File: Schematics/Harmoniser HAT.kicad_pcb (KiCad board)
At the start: 2 copper layers, 150 x 75 mm, 34 parts, among them J1 RPi GPIO, J10 Line In, J11 BOB21250-LEFT, J12 BOB21250-RIGHT, J6 I2C Header, J7 PWR, J8 I2S Header, J9 Line In, SW1 RotaryEncoder_Switch, SW2 RotaryEncoder_Switch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

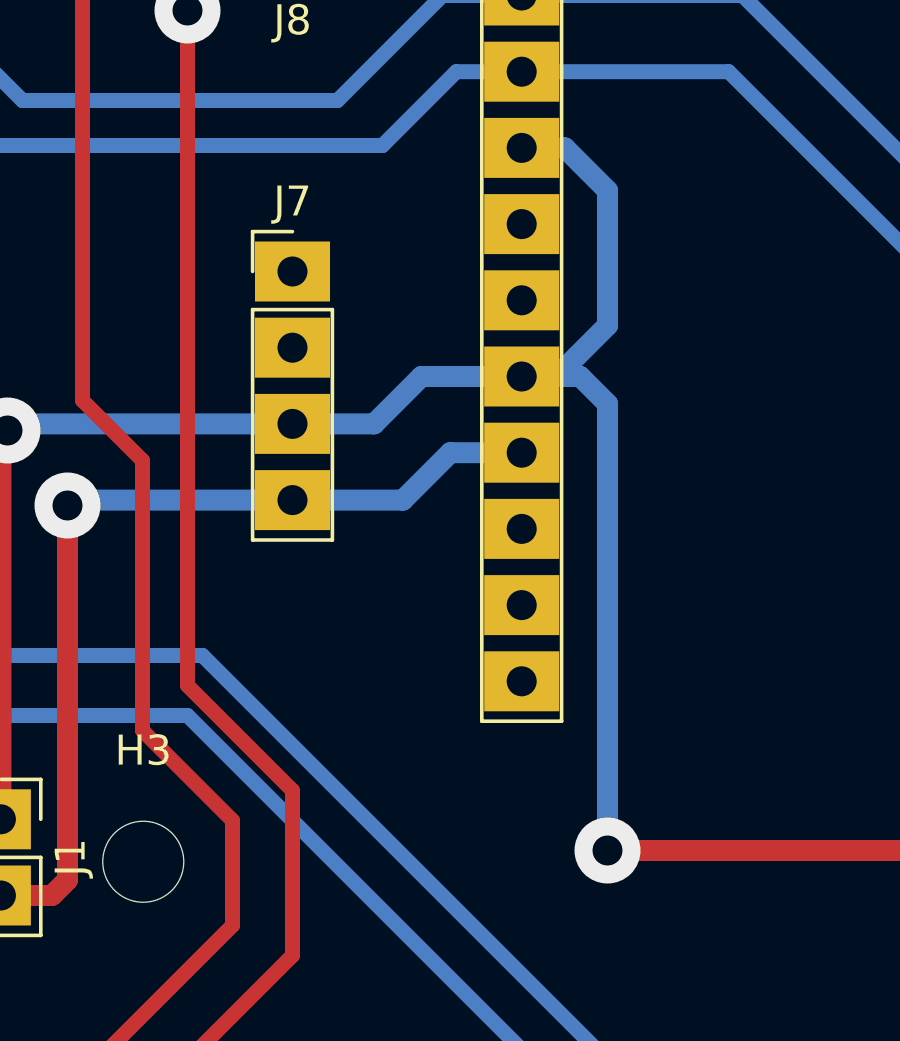
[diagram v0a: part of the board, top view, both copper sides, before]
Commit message: Fixed power connections on CODEC
So the codec board regulates its own AVDD which we had named but disconnected. In order for this regulation to happen the EN pin must be pulled high (not low as it says in the documentation).
SPKVDD was also disconnected as by default this is taken from VIN (5V) anyway, this means the CODEC boards don't need to be modified anymore.
Still need to test these on the board if time allows.
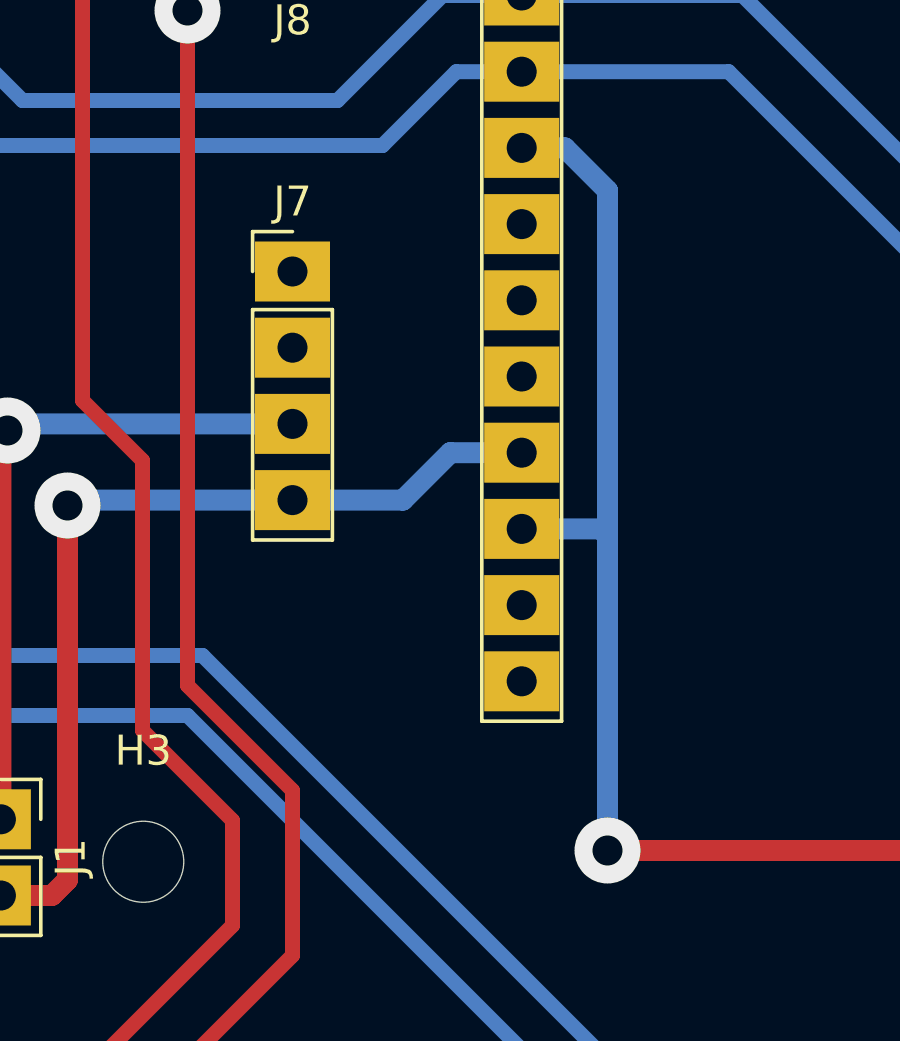
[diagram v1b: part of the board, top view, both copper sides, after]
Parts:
- J10: value Line In -> Line Out
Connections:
- C13 pad 1: OUT_L -> OUT_R
- C9 pad 1: OUT_R -> OUT_L
- J11 pad 12: +3V3 -> unconnected-(J11-Pin_12-Pad12)
- J11 pad 14: unconnected-(J11-Pin_14-Pad14) -> +3V3
- J12 pad 12: +3.3VA -> unconnected-(J12-Pin_12-Pad12)
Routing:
- net +3V3: track 291.9 -> 282.4 mm
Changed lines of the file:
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@@
 	(net 11 "RIN2")
 	(net 12 "LIN2")
-	(net 13 "unconnected-(J11-Pin_14-Pad14)")
+	(net 13 "unconnected-(J11-Pin_12-Pad12)")
 	(net 14 "EEPROM_SCL")
 	(net 15 "unconnected-(J1-Pin_32-Pad32)")
@@
 	(net 48 "unconnected-(J12-Pin_16-Pad16)")
 	(net 49 "unconnected-(J12-Pin_4-Pad4)")
-	(net 50 "+3.3VA")
+	(net 50 "unconnected-(J12-Pin_12-Pad12)")
 	(net 51 "unconnected-(J12-Pin_13-Pad13)")
 	(net 52 "unconnected-(J12-Pin_15-Pad15)")
@@
 			(layers "*.Cu" "*.Mask")
 			(remove_unused_layers no)
-			(net 6 "OUT_L")
+			(net 4 "OUT_R")
 			(pintype "passive")
 		)
@@
 			(layers "*.Cu" "*.Mask")
 			(remove_unused_layers no)
-			(net 50 "+3.3VA")
+			(net 50 "unconnected-(J12-Pin_12-Pad12)")
 			(pinfunction "Pin_12")
-			(pintype "passive")
+			(pintype "passive+no_connect")
 		)
 		(pad "13" thru_hole rect
@@
 			(layers "*.Cu" "*.Mask")
 			(remove_unused_layers no)
-			(net 4 "OUT_R")
+			(net 6 "OUT_L")
 			(pintype "passive")
 		)
@@
 			)
 		)
-		(property "Value" "Line In"
+		(property "Value" "Line Out"
 			(at 0 -10 0)
 			(layer "F.Fab")
@@
 			(layers "*.Cu" "*.Mask")
 			(remove_unused_layers no)
-			(net 1 "+3V3")
+			(net 13 "unconnected-(J11-Pin_12-Pad12)")
 			(pinfunction "Pin_12")
-			(pintype "passive")
+			(pintype "passive+no_connect")
 		)
 		(pad "13" thru_hole rect
@@
 			(layers "*.Cu" "*.Mask")
 			(remove_unused_layers no)
-			(net 13 "unconnected-(J11-Pin_14-Pad14)")
+			(net 1 "+3V3")
 			(pinfunction "Pin_14")
-			(pintype "passive+no_connect")
+			(pintype "passive")
 		)
 		(pad "15" thru_hole rect
@@
 	)
 	(segment
-		(start 218.5 55.5)
-		(end 218.5 52.5)
+		(start 150.58 71.08)
+		(end 152 72.5)
 		(width 0.7)
 		(layer "B.Cu")
@@
 	)
 	(segment
-		(start 204.5 81.5)
-		(end 204.5 89)
+		(start 218.5 55.5)
+		(end 218.5 52.5)
 		(width 0.7)
 		(layer "B.Cu")
@@
 	)
 	(segment
-		(start 141.5 80.28)
-		(end 144.22 80.28)
+		(start 204.5 81.5)
+		(end 204.5 89)
 		(width 0.7)
 		(layer "B.Cu")
@@
 	)
 	(segment
-		(start 144.22 80.28)
-		(end 145.8 78.7)
+		(start 149.14 71.08)
+		(end 150.58 71.08)
 		(width 0.7)
 		(layer "B.Cu")
@@
 	(segment
 		(start 152 94.5)
-		(end 152 79.61)
+		(end 152 84)
 		(width 0.7)
 		(layer "B.Cu")
@@
 	)
 	(segment
-		(start 145.8 78.7)
-		(end 149.14 78.7)
+		(start 180.34 49.5)
+		(end 177.34 52.5)
 		(width 0.7)
 		(layer "B.Cu")
@@
 	)
 	(segment
-		(start 180.34 49.5)
-		(end 177.34 52.5)
+		(start 132 80.5)
+		(end 132.22 80.28)
 		(width 0.7)
 		(layer "B.Cu")
@@
 	)
 	(segment
-		(start 132 80.5)
-		(end 132.22 80.28)
+		(start 152 72.5)
+		(end 152 84)
 		(width 0.7)
 		(layer "B.Cu")
@@
 	)
 	(segment
-		(start 152 79.61)
-		(end 151.09 78.7)
-		(width 0.7)
-		(layer "B.Cu")
-		(net 1)
-	)
-	(segment
 		(start 199.39 79.89)
 		(end 198 78.5)
@@
 	)
 	(segment
-		(start 152 72.5)
-		(end 152 77)
-		(width 0.7)
-		(layer "B.Cu")
-		(net 1)
-	)
-	(segment
 		(start 193 75.5)
 		(end 177.34 75.5)
@@
 	)
 	(segment
-		(start 150.3 78.7)
-		(end 149.14 78.7)
+		(start 152 84)
+		(end 151.78 83.78)
 		(width 0.7)
 		(layer "B.Cu")
@@
 	)
 	(segment
-		(start 151.09 78.7)
-		(end 149.14 78.7)
-		(width 0.7)
-		(layer "B.Cu")
-		(net 1)
-	)
-	(segment
 		(start 202.89 79.89)
 		(end 204.5 81.5)
@@
 	)
 	(segment
-		(start 150.58 71.08)
-		(end 152 72.5)
-		(width 0.7)
-		(layer "B.Cu")
-		(net 1)
-	)
-	(segment
-		(start 152 77)
-		(end 150.3 78.7)
-		(width 0.7)
-		(layer "B.Cu")
-		(net 1)
-	)
-	(segment
-		(start 149.14 71.08)
-		(end 150.58 71.08)
+		(start 151.78 83.78)
+		(end 149.14 83.78)
 		(width 0.7)
 		(layer "B.Cu")

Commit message: Fixed left and right output channels
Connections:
- C13 pad 1: OUT_R -> OUT_L
- C9 pad 1: OUT_L -> OUT_R
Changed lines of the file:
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@@
 			(layers "*.Cu" "*.Mask")
 			(remove_unused_layers no)
-			(net 4 "OUT_R")
+			(net 6 "OUT_L")
 			(pintype "passive")
 		)
@@
 			(layers "*.Cu" "*.Mask")
 			(remove_unused_layers no)
-			(net 6 "OUT_L")
+			(net 4 "OUT_R")
 			(pintype "passive")
 		)
